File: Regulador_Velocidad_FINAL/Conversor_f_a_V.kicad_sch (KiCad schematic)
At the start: 14 parts, among them J2 Bornera Señal de Entrada, Q1 BC848, U2 4040, U3 4070, U4 TL082

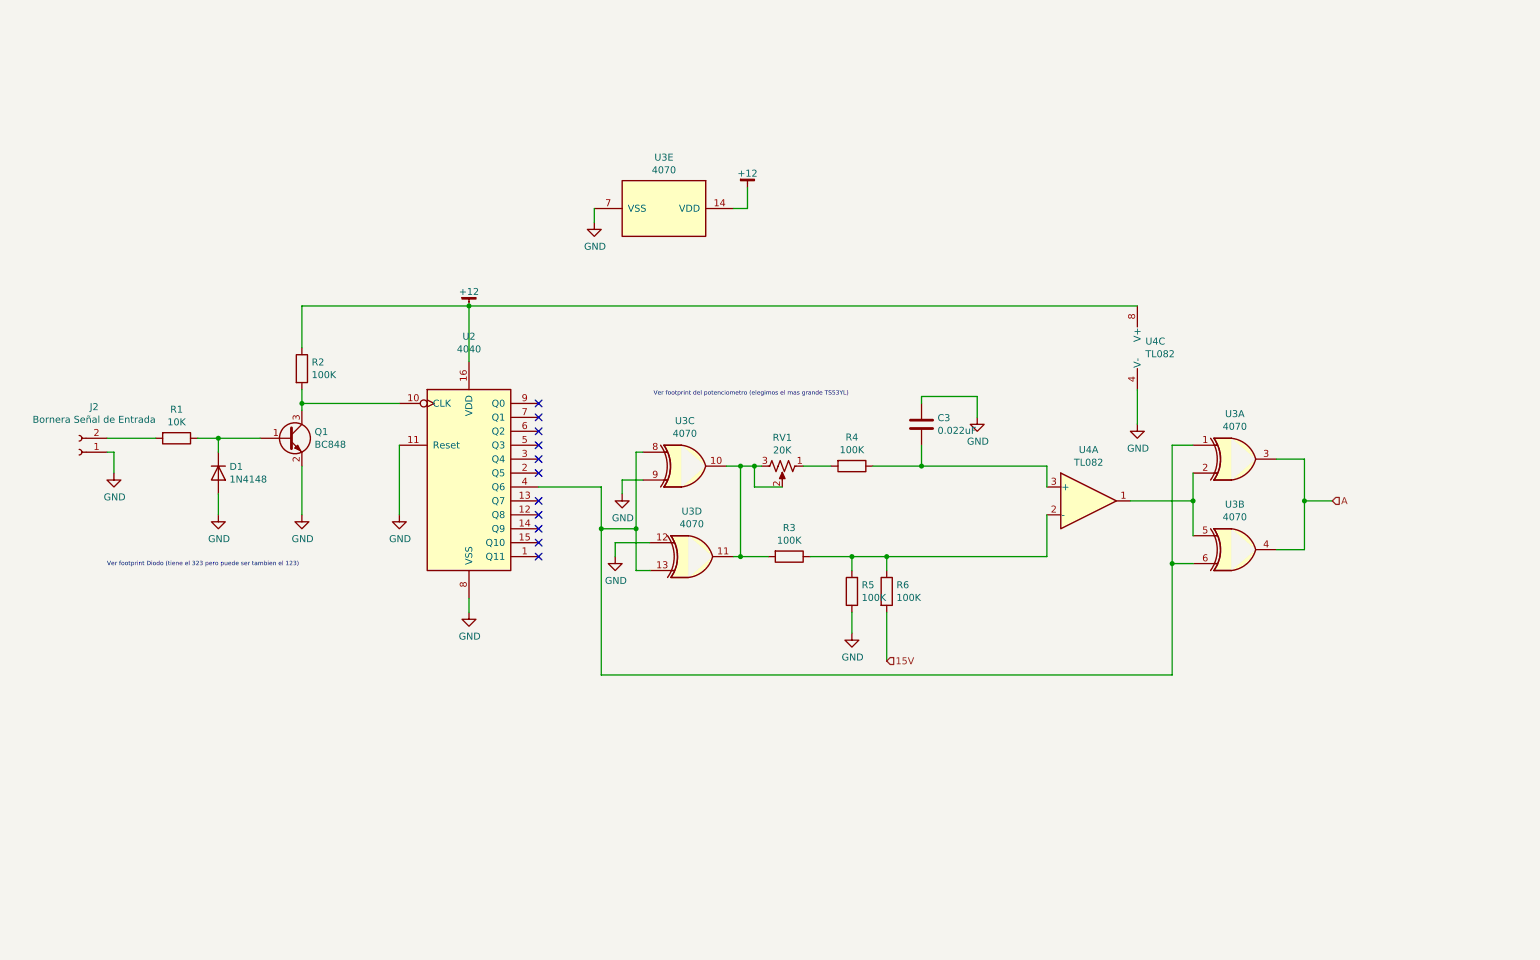
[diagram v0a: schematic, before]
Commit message: Monitor_speed: Changes Schematics
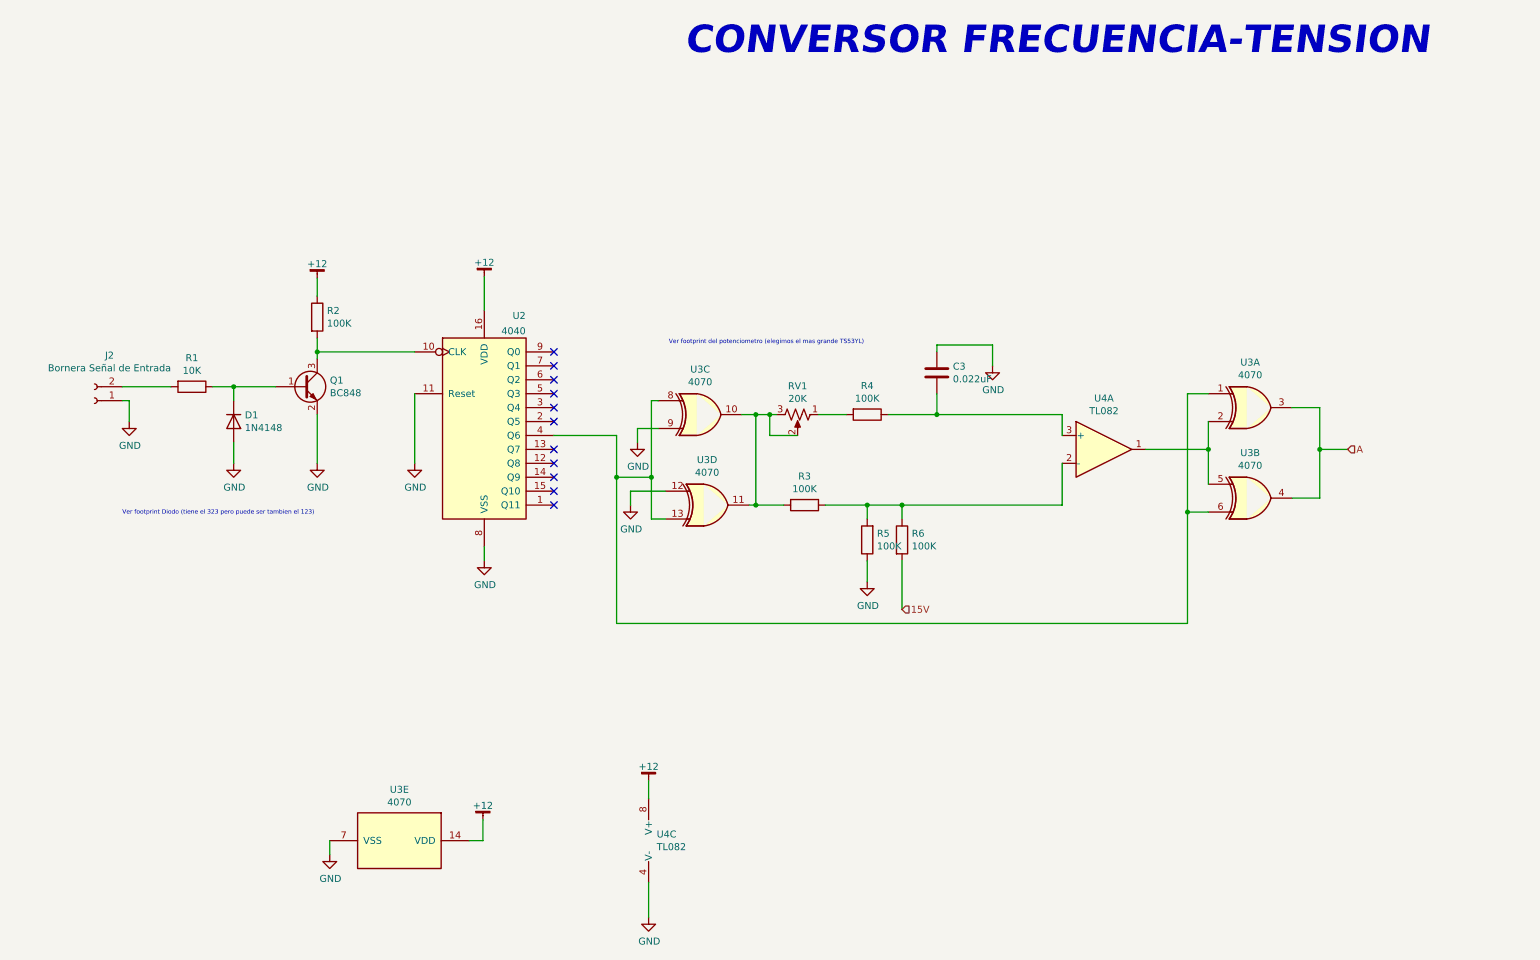
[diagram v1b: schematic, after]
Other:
- note added: "CONVERSOR FRECUENCIA-TENSION"
- moved on the sheet: C3, D1, J2, Q1, R1, R2, R3, R4, R5, R6, RV1, U2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

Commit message: Speed_Monitor: Changes on schematics
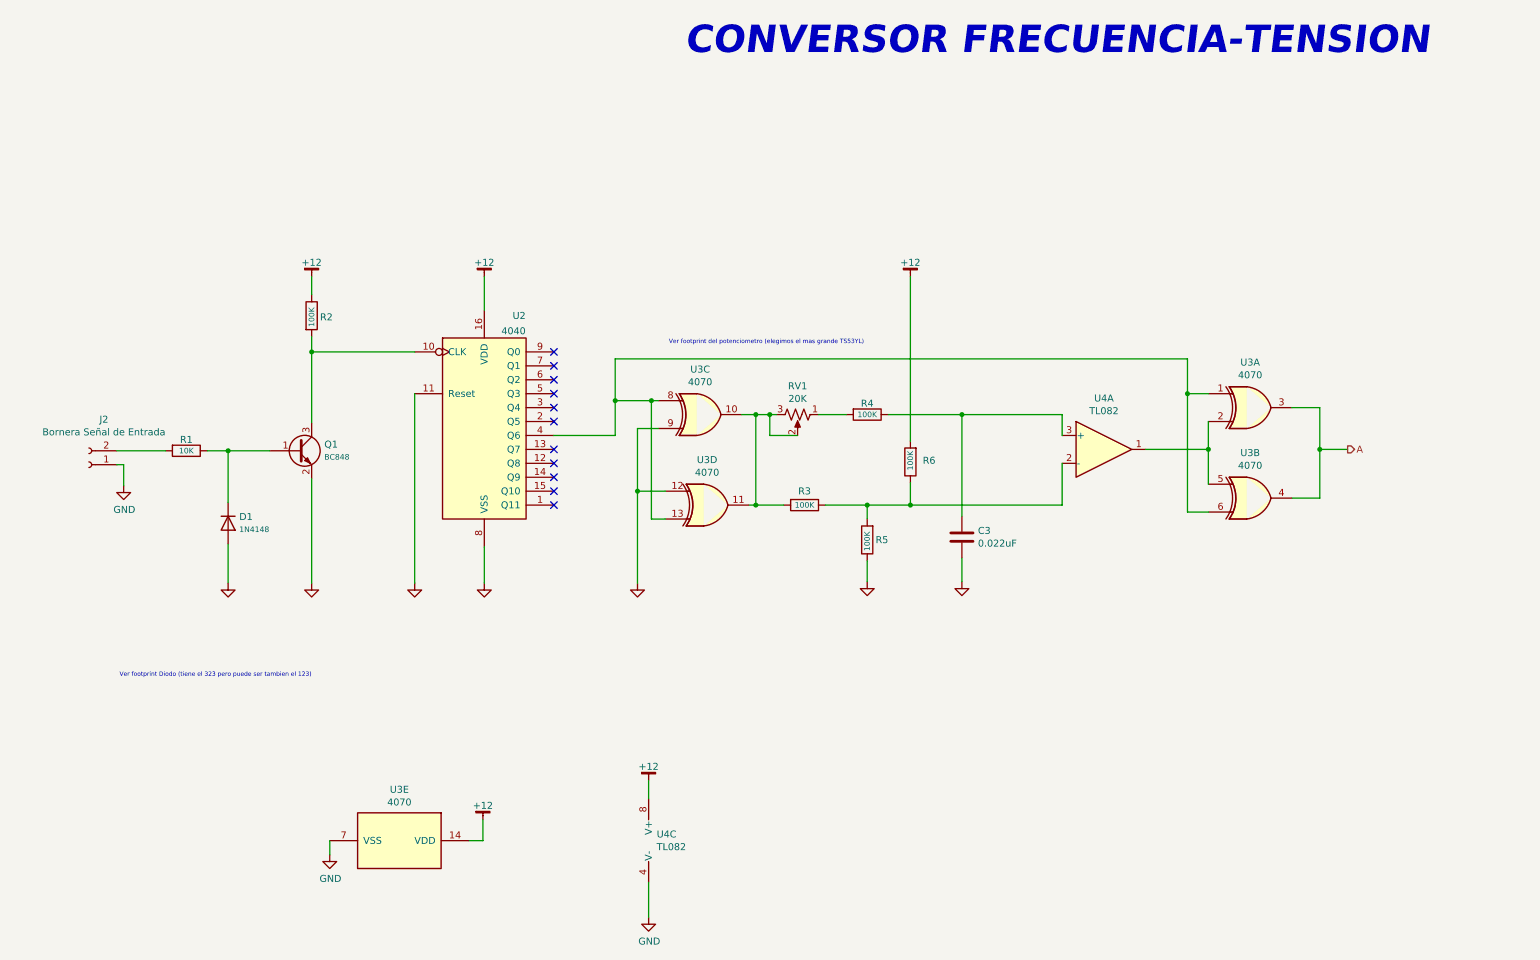
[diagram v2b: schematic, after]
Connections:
- net 15V is gone; now on net +12: R6.2
- net GND: now also C3.2; no longer C3.1
- net at R4.1, U4.3 (+): now also C3.1; no longer C3.2
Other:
- moved on the sheet: C3, D1, J2, Q1, R1, R2, R6
